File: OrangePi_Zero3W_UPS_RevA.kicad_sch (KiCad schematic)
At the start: 44 parts, among them J1 ORANGE_PI_ZERO_3W_HEADER, J2 BATTERY_1S_PROTECTED_NTC, J3 USB_C_POWER_INPUT, Q1 STL9P3LLH6, SW1 POWER / QON, U1 MAX17048G_T10, U2 BQ25895RTWR, U3 STUSB4500LQTR, U4 USBLC6-2SC6, U5 TPS61088RHLR

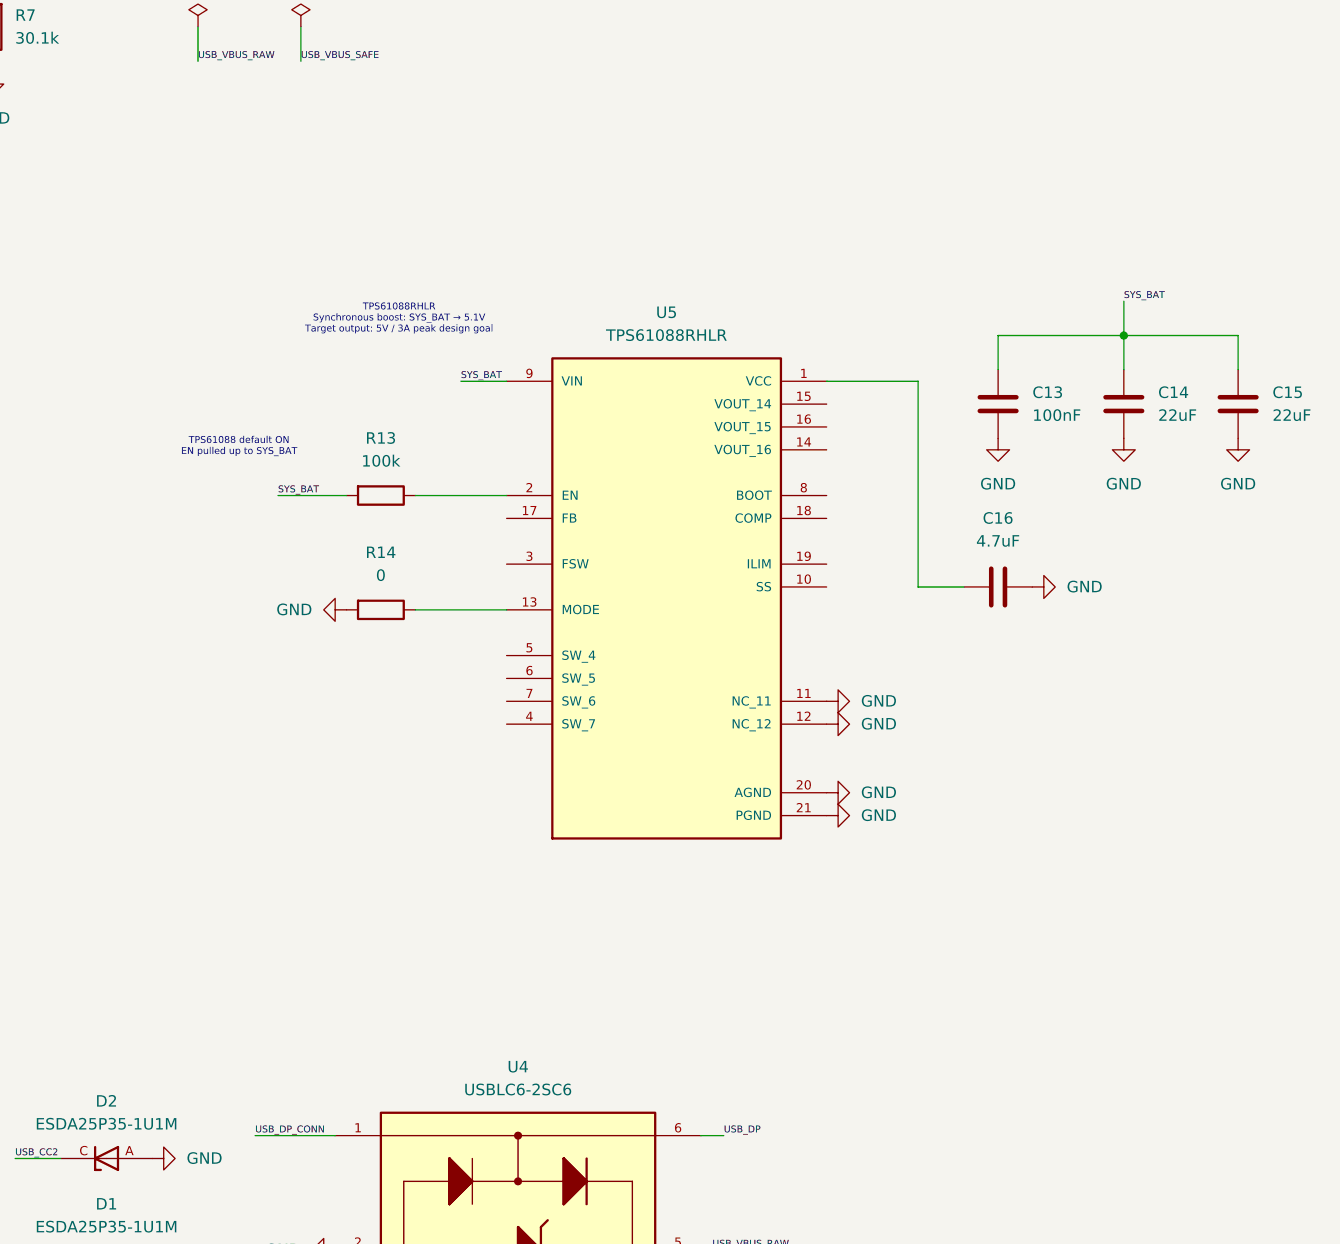
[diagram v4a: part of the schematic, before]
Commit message: Phase 5C.2B: add TPS61088 boost power stage and output capacitors
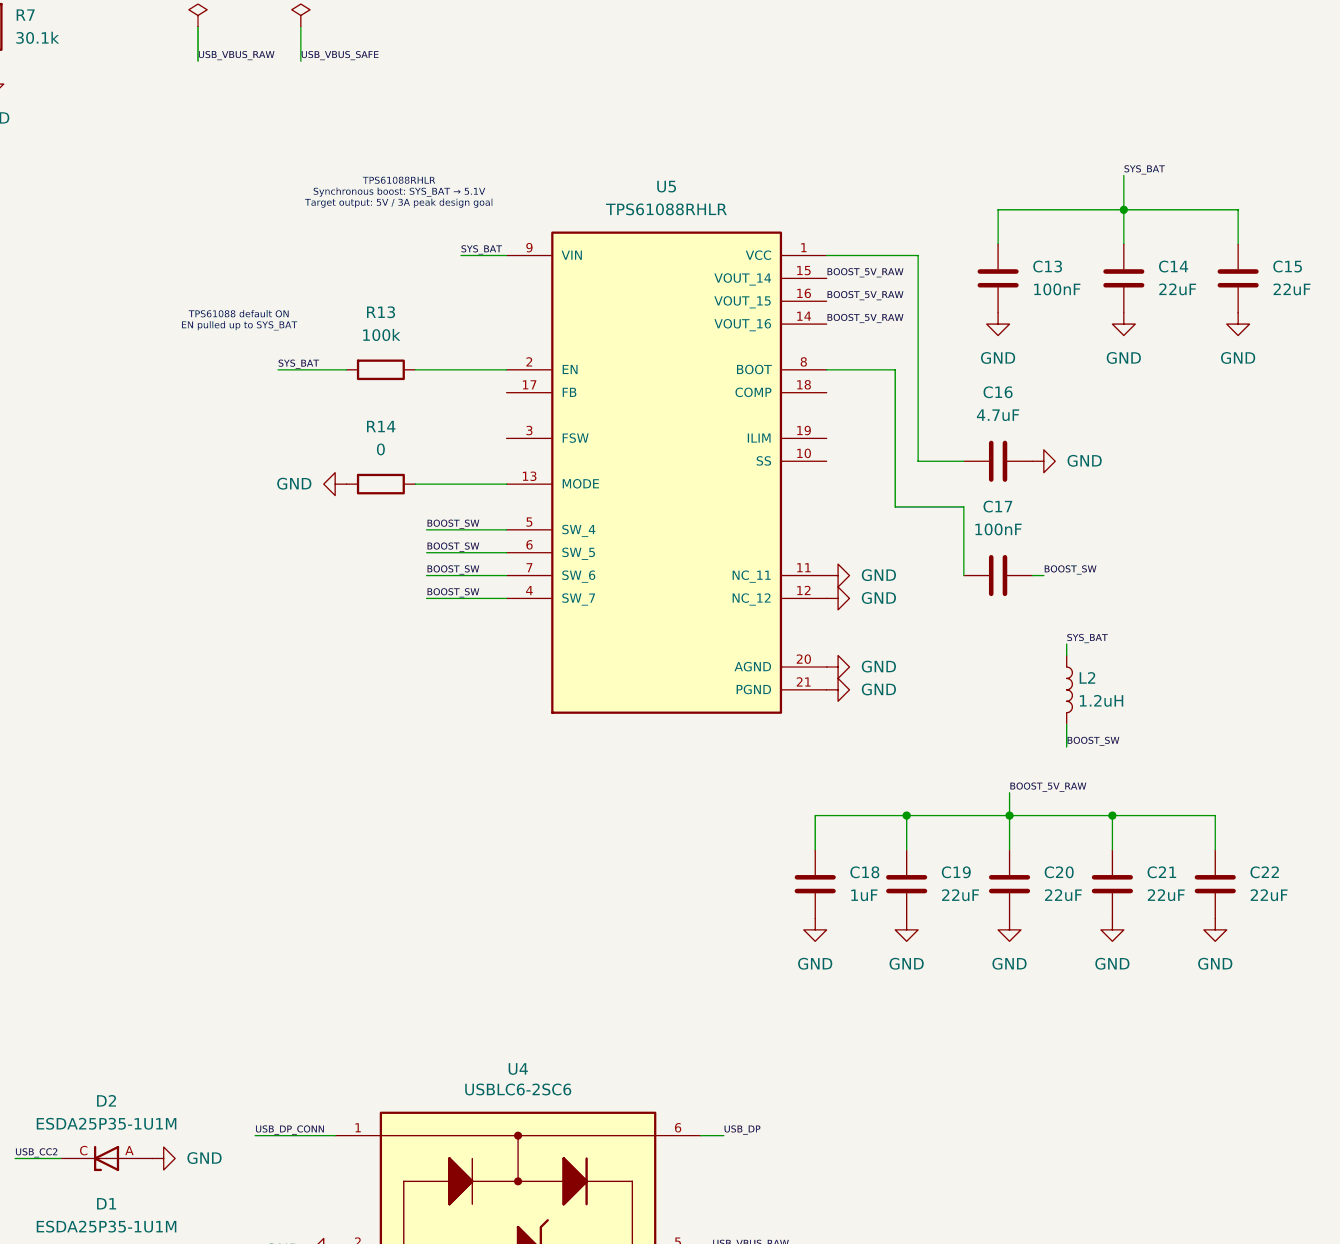
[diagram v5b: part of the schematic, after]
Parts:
- added C17: 100nF, Capacitor_SMD:C_0402_1005Metric, symbol Device:C
- added C18: 1uF, Capacitor_SMD:C_0603_1608Metric, symbol Device:C
- added C19, C20, C21, C22: 22uF, Capacitor_SMD:C_1206_3216Metric, symbol Device:C
- added L2: 1.2uH, symbol Device:L
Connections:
- net GND: now also C18.2, C19.2, C20.2, C21.2, C22.2
- net SYS_BAT: now also L2.1
- net BOOST_5V_RAW: now reaches U5.14 (VOUT_16)
- net BOOST_5V_RAW: now also U5.15 (VOUT_14), U5.16 (VOUT_15), C18.1, C19.1, C20.1, C21.1, C22.1
- net BOOST_SW: now reaches U5.4 (SW_7)
- net BOOST_SW: now also U5.5 (SW_4), U5.6 (SW_5), U5.7 (SW_6), C17.1, L2.2
- net at U5.8 (BOOT): now also C17.2
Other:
- moved on the sheet: C13, C14, C15, C16, R13, R14, U5

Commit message: Phase 5C.2B fix: normalize TPS61088 exposed pad to pin 21
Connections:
- net GND: no longer U5.22 (PGND), U5.23 (PGND), U5.24 (PGND), U5.25 (PGND), U5.26 (PGND), U5.27 (PGND), U5.28 (PGND), U5.29 (PGND)
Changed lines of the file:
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@@
 		(pin "20"
-		)
-		(pin "26"
 		)
 		(pin "2"
 		)
 		(pin "7"
-		)
-		(pin "24"
-		)
-		(pin "25"
-		)
-		(pin "22"
-		)
-		(pin "23"
 		)
 		(pin "6"
@@
 		(pin "21"
 		)
-		(pin "29"
-		)
-		(pin "27"
-		)
-		(pin "28"
-		)
 		(instances

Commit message: phase 5c.2c1
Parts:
- added C23: 47nF, Capacitor_SMD:C_0402_1005Metric, symbol Device:C
- added R15: 181k, Resistor_SMD:R_0603_1608Metric, symbol Device:R
- added R16: 56k, Resistor_SMD:R_0603_1608Metric, symbol Device:R
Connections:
- net BOOST_5V_RAW: now also R15.2
- net GND: now also C23.1, R16.2
- net at U5.10 (SS): now also C23.2
- net at U5.17 (FB): now also R15.1, R16.1
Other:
- moved on the sheet: L2

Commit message: Phase 5C.2C2: set TPS61088 switching frequency and current limit
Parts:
- added R17: 267k, Resistor_SMD:R_0603_1608Metric, symbol Device:R
- added R18: 100k, Resistor_SMD:R_0603_1608Metric, symbol Device:R
- R15, R16: Field5 1% -> (none); tolerance (none) -> 1%
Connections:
- net BOOST_SW: now also R17.1
- net GND: now also R18.2
- net at U5.19 (ILIM): now also R18.1
- net at U5.3 (FSW): now also R17.2
